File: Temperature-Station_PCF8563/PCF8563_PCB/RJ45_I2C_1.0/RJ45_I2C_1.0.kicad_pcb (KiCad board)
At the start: 2 copper layers, 28 parts, among them J0 MHRJJ66NFRA, J1 MHRJJ66NFRA, J2 MHRJJ66NFRA, J3 MHRJJ66NFRA, J4 MHRJJ66NFRA, J5 MHRJJ66NFRA, J6 MHRJJ66NFRA, J7 MHRJJ66NFRA, J8 Out, J9 Prog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

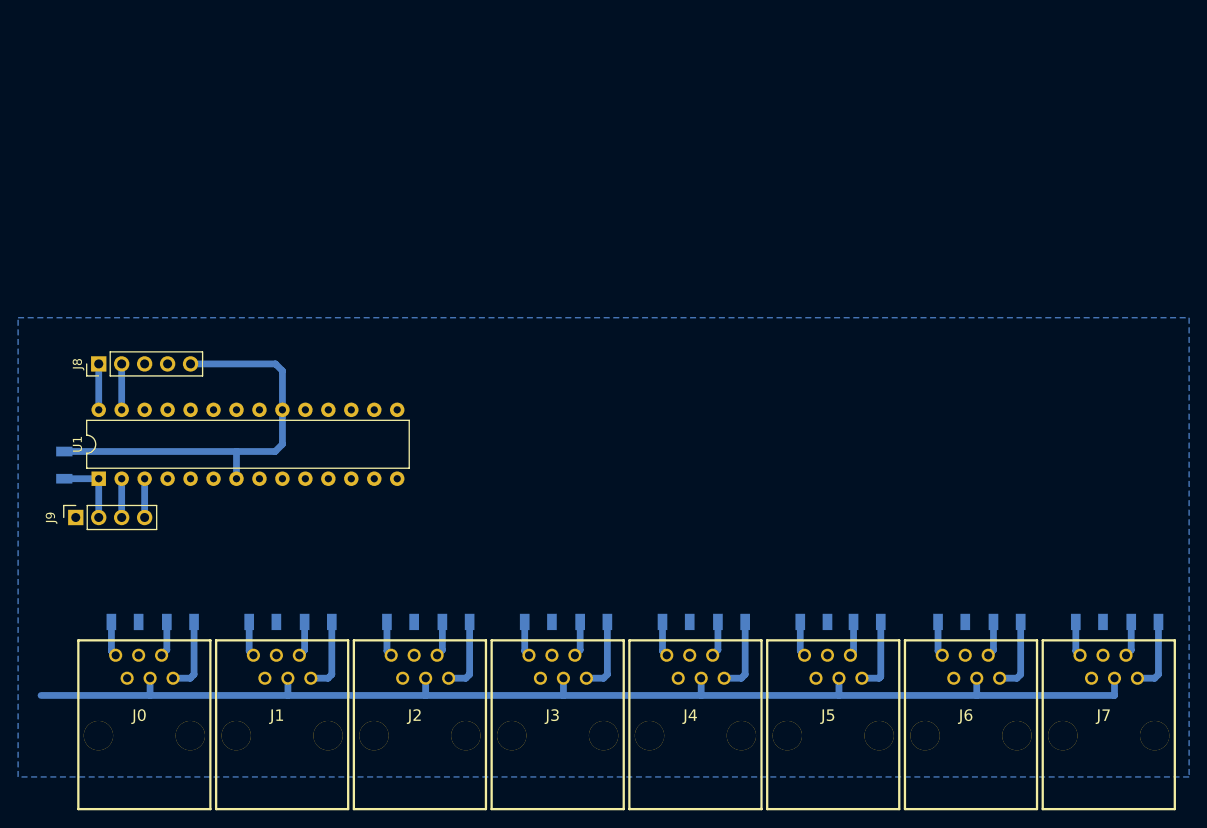
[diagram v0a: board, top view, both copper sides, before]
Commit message: Updated boards and sketches
Boards:
Sandwich-like layout so you can connect directly do DHT sensors or use i2c expansion (8 slots).
Boards support 1wire, DHT11/21/22 sensors and require custom wiring.
Reduced size of boards

Sketch:
Hermetized settings (no way to read passwords)
Used settingsHandler to hold every field that will have to be saved
Fixed AP launch in PCF8563
Rolled back Pinger library due to readability issues.
WIP: Use external memory only for emergency sensor file and permanently for readings
TESTING: Update via curl
TESTING: Set time and date via webpage
WIP: Change settings via webpage
WIP: Change login credentials via webpage
Documentation: coming soon
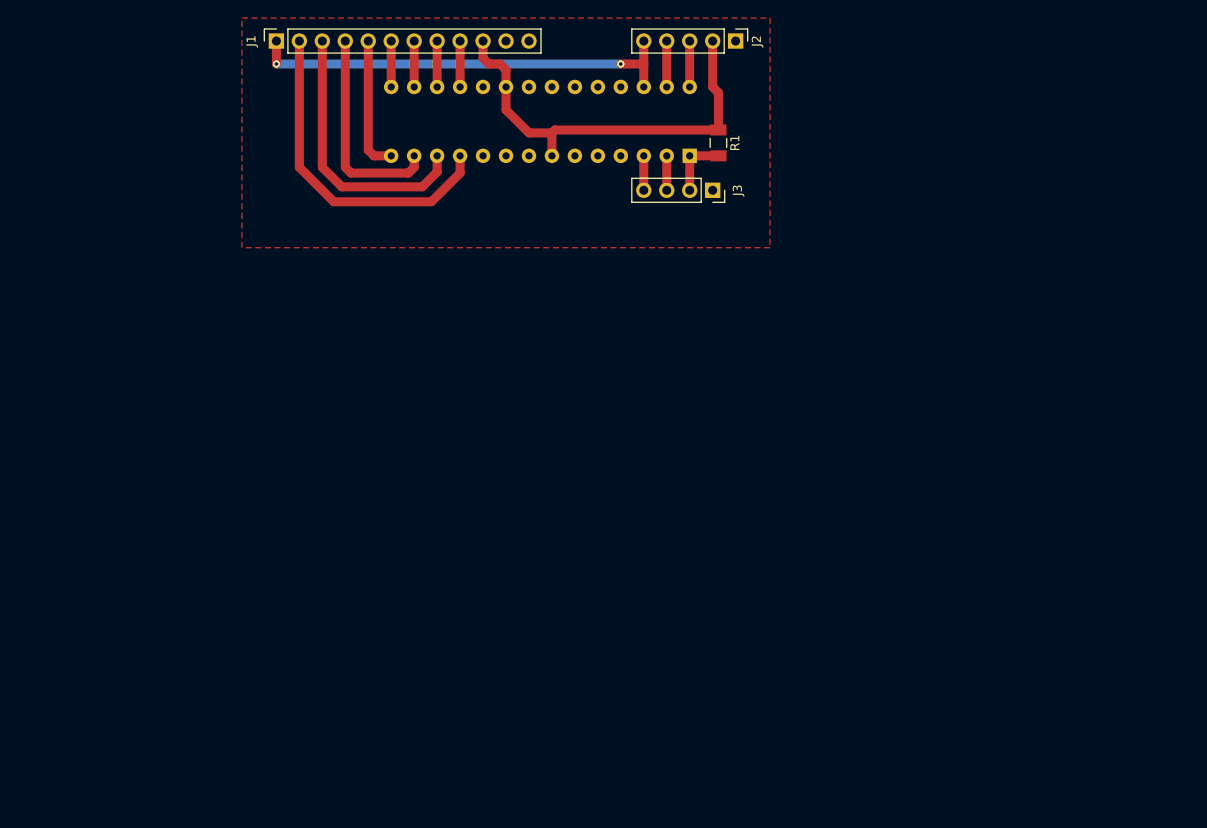
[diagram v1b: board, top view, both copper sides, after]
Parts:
- removed J0, J4, J5, J6, J7: MHRJJ66NFRA, MHRJJ66NFRA:MHRJJ66NFRA
- removed J8: Out, Connector_PinHeader_2.54mm:PinHeader_1x05_P2.54mm_Vertical
- removed J9: Prog, Connector_PinSocket_2.54mm:PinSocket_1x04_P2.54mm_Vertical
- removed R10, R11, R12, R13, R14, R15, R16, R17, R9: 10k, Resistor_SMD:R_1206_3216Metric
- removed R2, R3, R4, R5, R6, R7, R8: 4k7, Resistor_SMD:R_1206_3216Metric
- J1: value MHRJJ66NFRA -> Conn_01x12; footprint MHRJJ66NFRA:MHRJJ66NFRA -> Connector_PinSocket_2.54mm:PinSocket_1x12_P2.54mm_Vertical
- J2: value MHRJJ66NFRA -> Out; footprint MHRJJ66NFRA:MHRJJ66NFRA -> Connector_PinHeader_2.54mm:PinHeader_1x05_P2.54mm_Vertical
- J3: value MHRJJ66NFRA -> Prog; footprint MHRJJ66NFRA:MHRJJ66NFRA -> Connector_PinSocket_2.54mm:PinSocket_1x04_P2.54mm_Vertical
- R1: value 4k7 -> 10k; moved to F.Cu
- U1: moved to B.Cu
- moved R1 79.7 mm to (141.0, 69.1), turned to 270 degrees
- moved J2 76.4 mm to (142.9, 57.8), turned to 270 degrees
- moved U1 74.5 mm to (137.8, 70.5)
- moved J1 67.9 mm to (92.1, 57.8), turned to 90 degrees
- moved J3 54.2 mm to (140.3, 74.3), turned to 270 degrees
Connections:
- J1 pad 1: dht_1 -> 1wire
- J1 pad 2: GND -> dht_0
- J1 pad 3: GND -> dht_1
- J1 pad 4: 1wire -> dht_2
- J1 pad 5: Net-(J1-Pad5) -> dht_3
- J1 pad 6: 3V3 -> dht_4
- J1 pad 7: (no net) -> dht_5
- J1 pad 8: (no net) -> dht_6
- J2 pad 1: dht_2 -> GND
- J2 pad 2: GND -> 3V3
- J2 pad 3: GND -> SCL
- J2 pad 4: 1wire -> SDA
- J2 pad 5: Net-(J2-Pad5) -> 1wire
- J3 pad 1: dht_3 -> GND
- J3 pad 2: GND -> Net-(J3-Pad2)
- J3 pad 3: GND -> Net-(J3-Pad3)
- J3 pad 4: 1wire -> Net-(J3-Pad4)
- R1 pad 2: Net-(J0-Pad5) -> Net-(J3-Pad2)
- U1 pad 1: Net-(J9-Pad2) -> Net-(J3-Pad2)
- U1 pad 2: Net-(J9-Pad3) -> Net-(J3-Pad3)
- U1 pad 26: Net-(U1-Pad26) -> 1wire
- U1 pad 3: Net-(J9-Pad4) -> Net-(J3-Pad4)
- U1 pad 4: 1wire -> Net-(U1-Pad4)
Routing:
- net 1wire: track 134.0 -> 48.3 mm, vias 0 -> 2
- net 3V3: track 112.4 -> 46.7 mm
- net dht_0: track 3.88 -> 36.5 mm
- net dht_1: track 3.88 -> 30.0 mm
- net dht_2: track 3.88 -> 23.4 mm
- net dht_3: track 3.88 -> 14.9 mm
- net Net-(J9-Pad2): track 8.10 -> 0.00 mm
- net Net-(J3-Pad2): track 0.00 -> 6.99 mm
- net Net-(J9-Pad4): track 4.29 -> 0.00 mm
- net Net-(J9-Pad3): track 4.29 -> 0.00 mm
- net Net-(J7-Pad5): track 3.93 -> 0.00 mm
- net Net-(J6-Pad5): track 3.93 -> 0.00 mm
- net Net-(J4-Pad5): track 3.93 -> 0.00 mm
- net Net-(J3-Pad5): track 3.93 -> 0.00 mm
- net Net-(J2-Pad5): track 3.93 -> 0.00 mm
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- added copper zone on F.Cu, net GND
- removed copper zone on B.Cu, net GND
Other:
- net class Default: trace_width 0.75 -> 1
- net class Grubsze removed

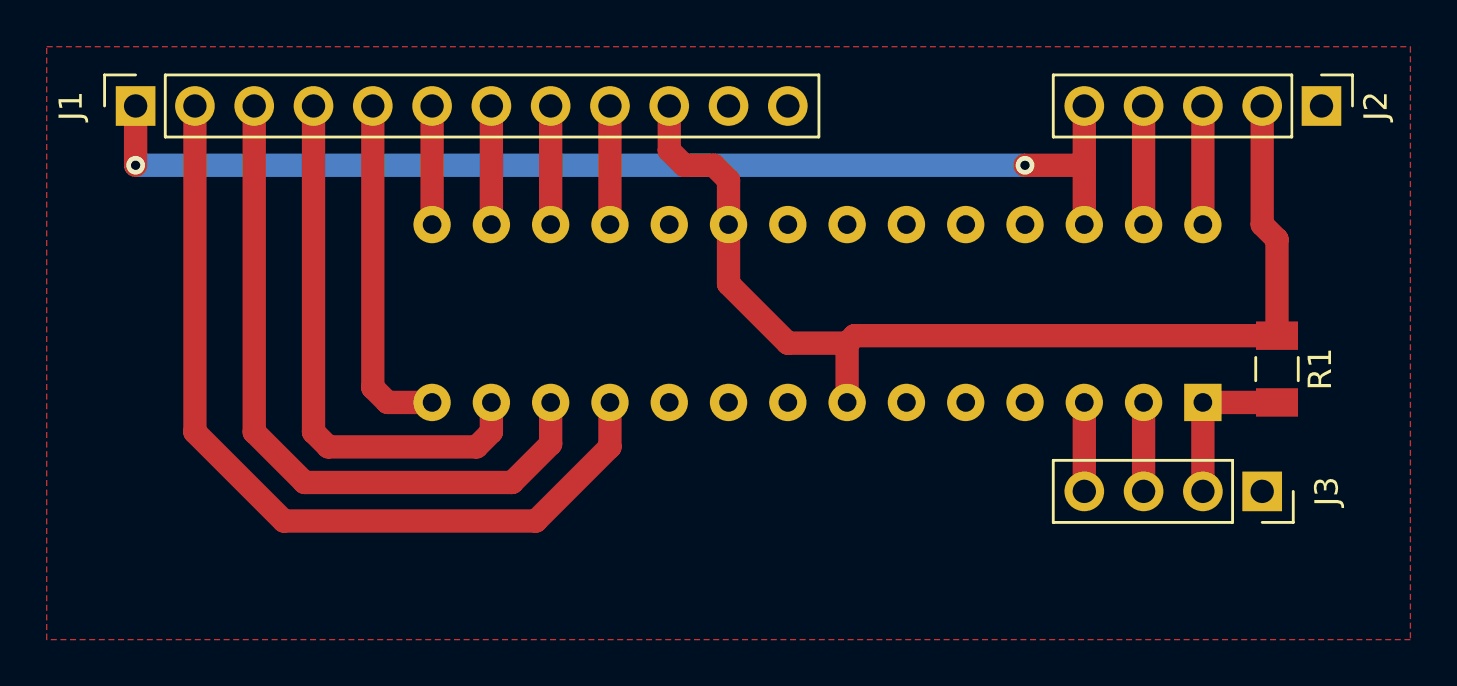
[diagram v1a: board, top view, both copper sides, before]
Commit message: Muxtemp update
1wire option added
Working in bypass or local mode (if master can use 1wire it will NOT use 1wire devices)
Example shows more info
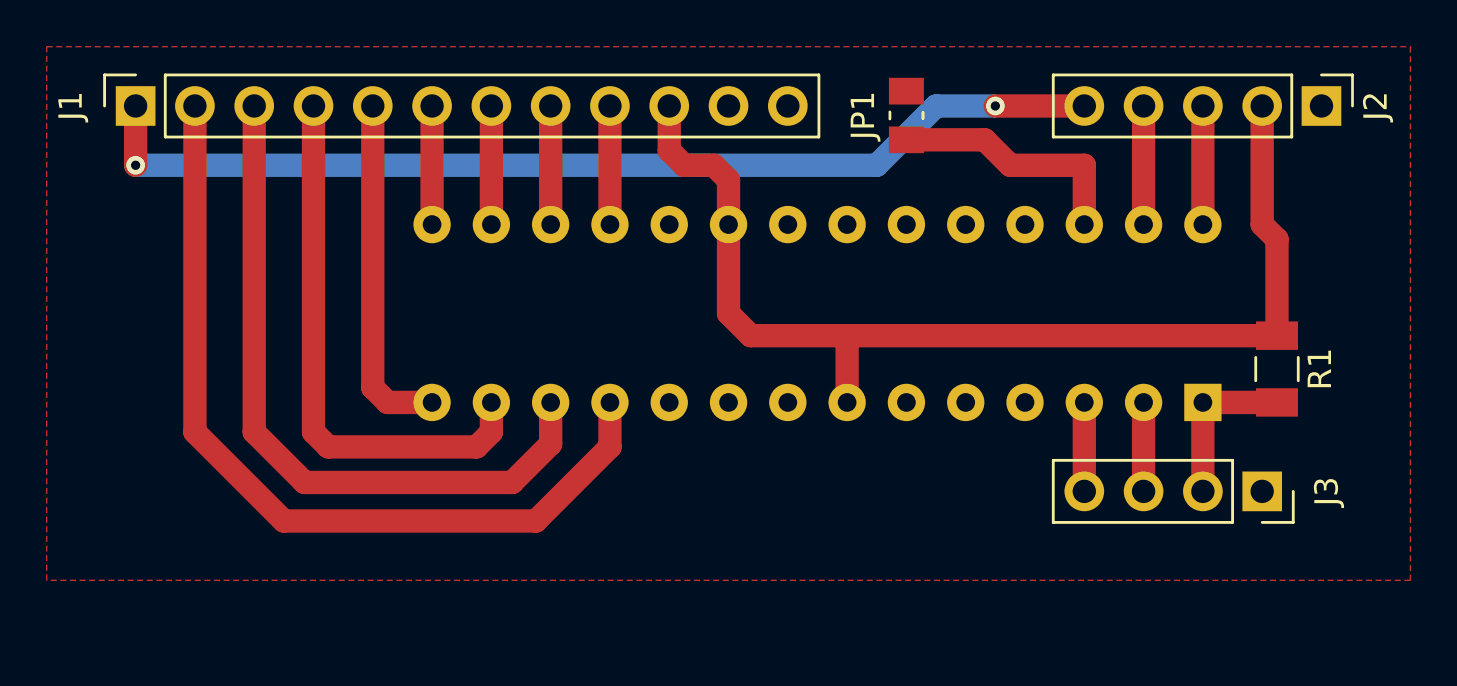
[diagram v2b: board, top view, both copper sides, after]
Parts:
- added JP1: bypass1Wire, Resistor_SMD:R_0805_2012Metric_Pad1.15x1.50mm_HandSolder, F.Cu at (125.1, 58.2)
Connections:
- U1 pad 26: 1wire -> Net-(JP1-Pad1)
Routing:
- net Net-(JP1-Pad1): track 0.00 -> 10.6 mm
- net 1wire: track 48.3 -> 44.2 mm
- net 3V3: track 46.7 -> 47.5 mm
